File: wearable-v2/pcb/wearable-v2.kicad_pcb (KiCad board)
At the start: 2 copper layers, 112.1 x 40.2 mm, 90 parts, among them IC1 TESEO-LIV3F, J1 HERALD_V2_CONN_RECEPTACLE, J2 HERALD_V2_CONN_RECEPTACLE, J3 HERALD_V2_CONN_RECEPTACLE, J4 HERALD_V2_CONN_RECEPTACLE, J5 HERALD_V2_CONN_PORT, J6 HERALD_V2_CONN_PORT, J7 USB_C_Receptacle_USB2.0, J8 HERALD_V2_CONN_PORT, J9 HERALD_V2_CONN_PORT, SW1 SW_Push, U1 DT1446-04V, U10 ATmega328PB-M, U11 TMP1075, U12 MAX30102, U14 LIS2DE12, U15 TLV751, U2 MCP73831/2-2MC, U3 TCA6408A, U4 FT201XQ, U6 BC833, U7 MX25R8035FZxxx0, U8 PCF85063ATL, U9 APDS-9250, Y1 32.768kHz

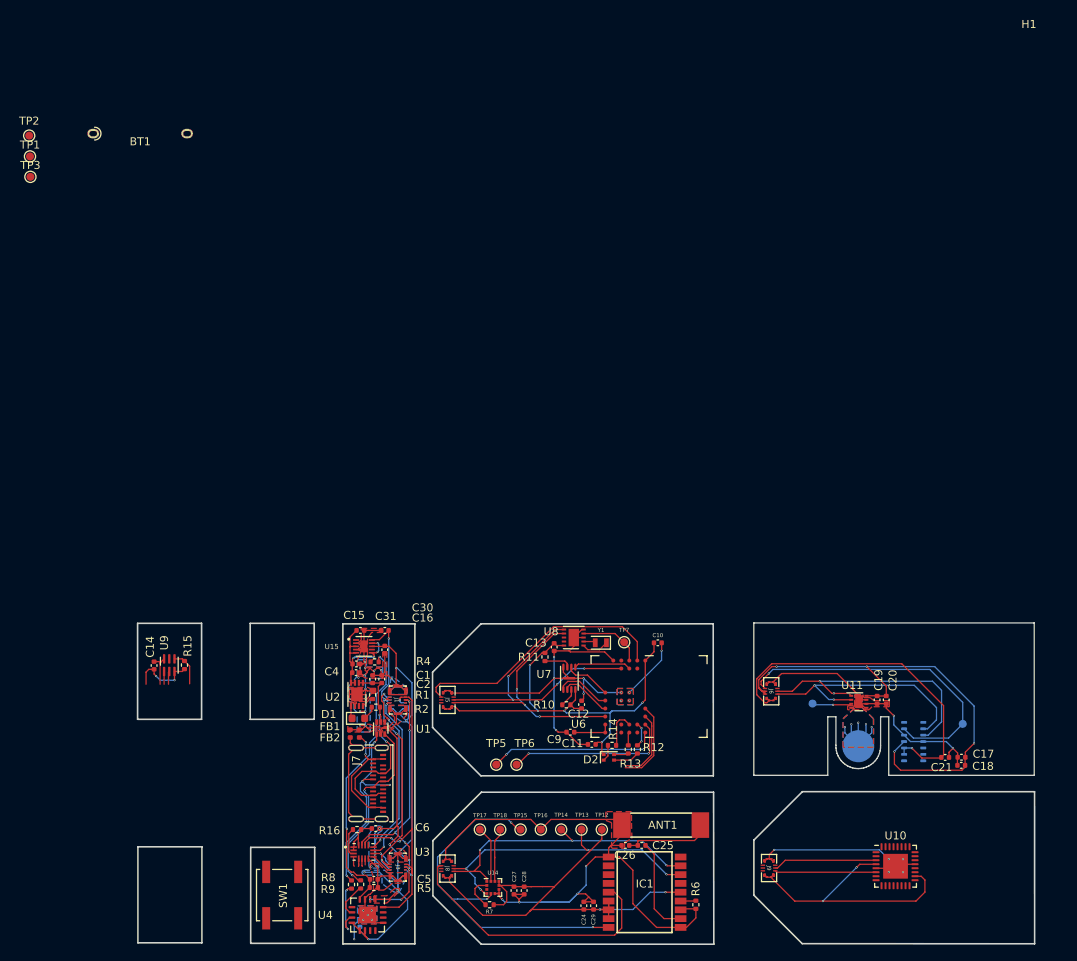
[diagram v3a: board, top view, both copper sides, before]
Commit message: Set wider PCB GND tracks and vias
Signed-off-by: Adam Fowler <adam@adamfowler.org>
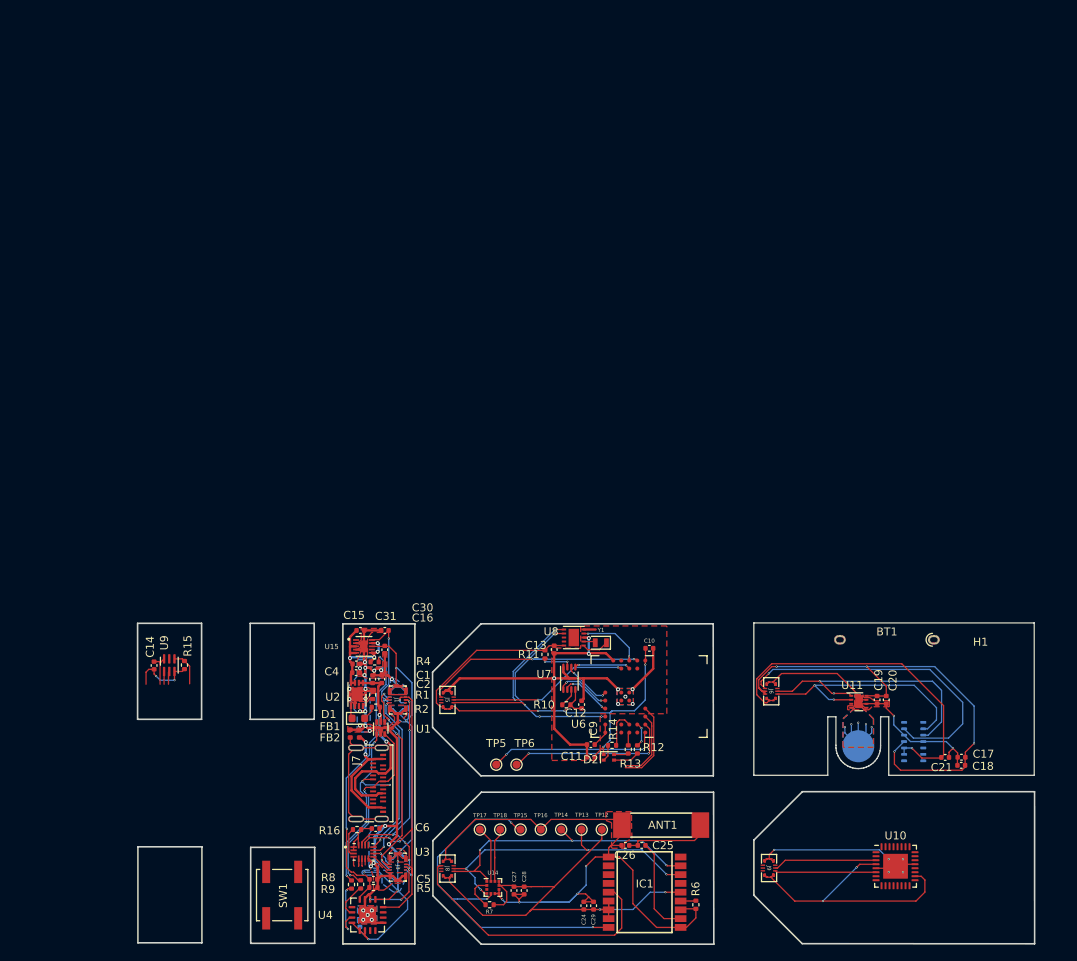
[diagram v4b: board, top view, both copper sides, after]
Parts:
- removed TP1: VBUS, TestPoint:TestPoint_Pad_D1.0mm
- removed TP11: BIOINT, TestPoint:TestPoint_Pad_D1.0mm
- removed TP2: GND, TestPoint:TestPoint_Pad_D1.0mm
- removed TP3: BTSTAT, TestPoint:TestPoint_Pad_D1.0mm
- removed TP7: RTCINT, TestPoint:TestPoint_Pad_D1.0mm
- removed TP8: TMPINT, TestPoint:TestPoint_Pad_D1.0mm
- moved BT1 112.8 mm to (159.3, 101.2), turned to 180 degrees
- moved H1 77.5 mm to (171.0, 103.1)
- moved C9 3.00 mm to (122.3, 114.4)
- moved C11 1.60 mm to (122.3, 115.9)
- moved C10 1.26 mm to (129.6, 102.3)
- moved R11 0.32 mm to (116.5, 103.1)
- moved C13 0.30 mm to (117.7, 102.5)
- moved C5 0.05 mm to (95.1, 131.2)
- moved R5 0.05 mm to (95.1, 132.2)
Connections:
- U8 pad EP: GND -> (no net)
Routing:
- net VDD: track 288.7 -> 297.4 mm, vias 19 -> 18
- net /Bio Board V1/TMP_INT: track 4.95 -> 0.00 mm, vias 1 -> 0
- net GND: track 333.8 -> 329.6 mm, vias 53 -> 49
- net /Compute - Fanstel BC833M - Nordic Semi nRF52833 based/EXT_INT1: track 54.4 -> 50.3 mm, vias 2 -> 4
- net VBUS: track 30.7 -> 28.8 mm
- net /Compute - Fanstel BC833M - Nordic Semi nRF52833 based/FLASH_WP: track 3.38 -> 3.89 mm, vias 0 -> 2
- net /Compute - Fanstel BC833M - Nordic Semi nRF52833 based/MISO: track 5.83 -> 6.21 mm, vias 0 -> 2
- net /Bio Board V1/SCL: track 155.1 -> 155.3 mm, vias 12 -> 13
- net /Compute - Fanstel BC833M - Nordic Semi nRF52833 based/SCLK: track 6.50 -> 6.60 mm, vias 0 -> 2
- net /Compute - Fanstel BC833M - Nordic Semi nRF52833 based/FLASH_CS: track 7.13 -> 7.05 mm, vias 0 -> 2
- net /Compute - Fanstel BC833M - Nordic Semi nRF52833 based/RTC_INT: track 8.04 -> 8.08 mm, vias 0 -> 2
- net /Compute - Fanstel BC833M - Nordic Semi nRF52833 based/MOSI: track 6.93 -> 6.95 mm, vias 0 -> 2

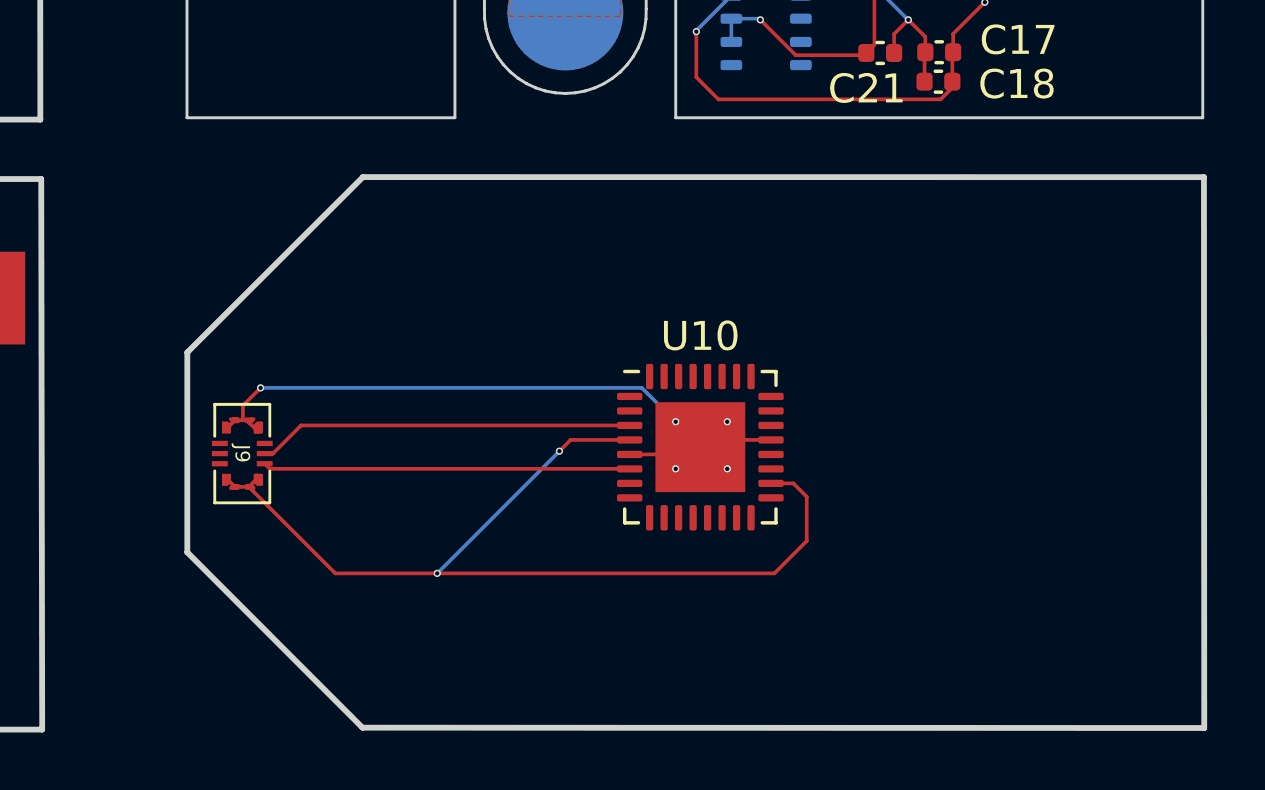
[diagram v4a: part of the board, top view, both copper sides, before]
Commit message: Display board physical layout improvements
Signed-off-by: Adam Fowler <adam@adamfowler.org>
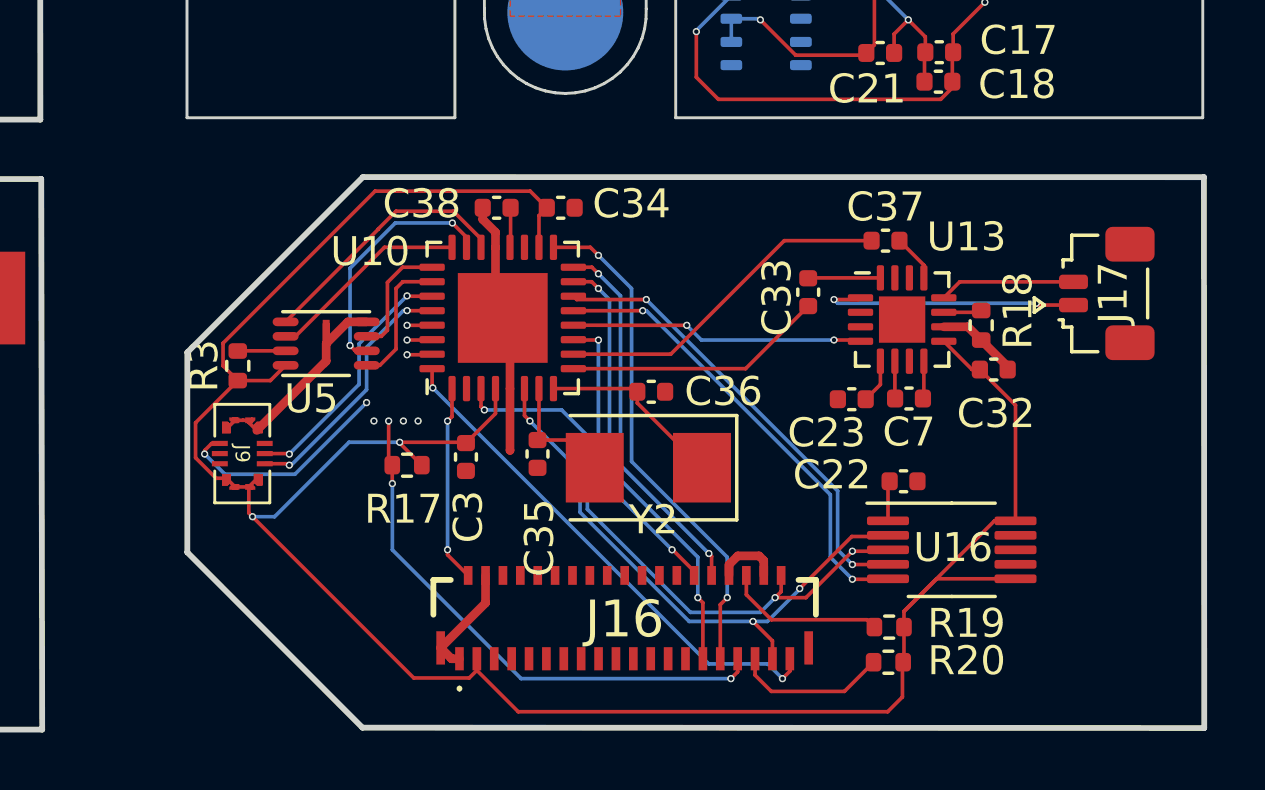
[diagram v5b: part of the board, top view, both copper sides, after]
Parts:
- added C22: 1uF 0402, Capacitor_SMD:C_0402_1005Metric, F.Cu at (167.4, 130.7)
- added C23: 1uF 0402, Capacitor_SMD:C_0402_1005Metric, F.Cu at (165.6, 127.9)
- added C3: 100nF 0402, Capacitor_SMD:C_0402_1005Metric, F.Cu at (152.3, 129.9)
- added C32: 1uF 0402, Capacitor_SMD:C_0402_1005Metric, F.Cu at (170.5, 126.9)
- added C33: 2.2uF 0402, Capacitor_SMD:C_0402_1005Metric, F.Cu at (164.1, 124.2)
- added C34: 10uF 0402, Capacitor_SMD:C_0402_1005Metric, F.Cu at (155.5, 121.3)
- added C35: 22pF 0402, Capacitor_SMD:C_0402_1005Metric, F.Cu at (154.7, 129.8)
- added C36: 22pF 0402, Capacitor_SMD:C_0402_1005Metric, F.Cu at (158.7, 127.6)
- added C37: 2.2uF 0402, Capacitor_SMD:C_0402_1005Metric, F.Cu at (166.8, 122.4)
- added C38: 100nF 0402, Capacitor_SMD:C_0402_1005Metric, F.Cu at (153.3, 121.3)
- added C7: 1uF 0402, Capacitor_SMD:C_0402_1005Metric, F.Cu at (167.6, 127.9)
- added J16: EA_WF030-39S, Herald:EAWF03039S, F.Cu at (157.7, 135.7)
- added J17: Conn_01x02_Pin, Connector_JST:JST_SUR_SM02B-SURS-TF_1x02-1MP_P0.80mm_Horizontal, F.Cu at (174.4, 124.2)
- added R17: 1k 0402, Resistor_SMD:R_0402_1005Metric, F.Cu at (150.2, 130.2)
- added R18: 49.9k 0402, Resistor_SMD:R_0402_1005Metric, F.Cu at (170.1, 125.3)
- added R19: 10k 0402, Resistor_SMD:R_0402_1005Metric, F.Cu at (166.9, 135.8)
- added R20: 10k 0402, Resistor_SMD:R_0402_1005Metric, F.Cu at (166.8, 137.0)
- added R3: 10k, Resistor_SMD:R_0402_1005Metric, F.Cu at (144.4, 126.7)
- added U13: TPA6139A2RGTR, Package_DFN_QFN:TQFN-16-1EP_3x3mm_P0.5mm_EP1.6x1.6mm, F.Cu at (167.3, 125.2)
- added U16: DRV2605LDGS, Package_SO:VSSOP-10_3x3mm_P0.5mm, F.Cu at (169.0, 133.1)
- added U5: MX25R8035FZxxx0, Herald:USON-8-1EP_2x3mm_P0.5mm_EP0.25x1.65mm, F.Cu at (147.4, 126.0)
- added Y2: 8Mhz, Crystal:Crystal_SMD_5032-2Pin_5.0x3.2mm, F.Cu at (158.6, 130.3)
- moved U10 8.15 mm to (153.5, 125.1), turned to 90 degrees
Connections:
- net /Display Board V1/SOUND_PWM renamed /Display Board V1/FB_FTDI_TX
- net /Display Board V1/SS1 renamed /Display Board V1/FB_SS1
- ANT1 pad 2: GND -> (no net)
- J4 pad 6: /Display Board V1/INT_4 -> /Display Board V1/TOUCH_INT
- U10 pad 1: unconnected-(U10-PD3-Pad1) -> /Display Board V1/DISP_LED+
- U10 pad 10: /Display Board V1/VIBRATE_PWM -> /Display Board V1/FB_AUDIO_PWM_RIGHT
- U10 pad 11: unconnected-(U10-PD7-Pad11) -> /Display Board V1/DISP_CSX
- U10 pad 12: unconnected-(U10-PB0-Pad12) -> /Display Board V1/FB_AUDIO_SEL
- U10 pad 13: unconnected-(U10-PB1-Pad13) -> /Display Board V1/FB_VIBRATE_EN
- U10 pad 14: /Display Board V1/CSX -> /Display Board V1/FB_VIBRATE_PWM
- U10 pad 15: /Display Board V1/MOSI0 -> /Display Board V1/DISP_SDA
- U10 pad 16: /Display Board V1/MISO0 -> /Display Board V1/DISP_SDO
- U10 pad 17: /Display Board V1/DCX -> /Display Board V1/DISP_DCX
- U10 pad 20: unconnected-(U10-AREF-Pad20) -> Net-(U10-AREF)
- U10 pad 22: /Display Board V1/MOSI1 -> /Display Board V1/FB_MOSI1
- U10 pad 23: /Display Board V1/MISO1 -> /Display Board V1/FB_MISO1
- U10 pad 24: /Display Board V1/SCK1 -> /Display Board V1/FB_SCK1
- U10 pad 25: /Display Board V1/LED+ -> /Display Board V1/FB_FLASH_WP
- U10 pad 26: unconnected-(U10-PC3-Pad26) -> /Display Board V1/FB_FLASH_SEL
- U10 pad 29: /Display Board V1/AVR_RESET -> /Display Board V1/DISP_RESET
- U10 pad 3: /Bio Board V1/SDA -> /Display Board V1/FB_SDA
- U10 pad 31: unconnected-(U10-PD1-Pad31) -> /Display Board V1/FB_FTDI_RX
- U10 pad 32: /Display Board V1/INT_4 -> /Display Board V1/TOUCH_INT
- U10 pad 6: /Bio Board V1/SCL -> /Display Board V1/FB_SCL
- U10 pad 7: unconnected-(U10-XTAL1/PB6-Pad7) -> Net-(U10-XTAL1/PB6)
- U10 pad 8: unconnected-(U10-XTAL2/PB7-Pad8) -> Net-(U10-XTAL2/PB7)
- U10 pad 9: unconnected-(U10-PD5-Pad9) -> /Display Board V1/FB_AUDIO_PWM_LEFT
- U15 pad 11: GND -> (no net)
- U2 pad 9: GND -> (no net)
- U3 pad 10: /Display Board V1/INT_4 -> /Display Board V1/TOUCH_INT
- U8 pad EP: (no net) -> unconnected-(U8-PadEP)
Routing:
- net VDD: track 297.4 -> 347.3 mm
- net /Display Board V1/FB_SDA: track 0.00 -> 20.9 mm, vias 0 -> 3
- net /Display Board V1/TOUCH_INT: track 0.00 -> 20.5 mm, vias 0 -> 3
- net /Display Board V1/FB_SCL: track 0.00 -> 20.1 mm, vias 0 -> 3
- net /Display Board V1/DISP_RESET: track 0.00 -> 19.7 mm, vias 0 -> 4
- net /Display Board V1/DISP_DCX: track 0.00 -> 17.5 mm, vias 0 -> 2
- net /Display Board V1/FB_VIBRATE_EN: track 0.00 -> 16.0 mm, vias 0 -> 2
- net /Display Board V1/FB_VIBRATE_PWM: track 0.00 -> 15.9 mm, vias 0 -> 2
- net /Display Board V1/DISP_SDA: track 0.00 -> 15.2 mm, vias 0 -> 2
- net /Display Board V1/DISP_SDO: track 0.00 -> 13.0 mm, vias 0 -> 2
- net /Display Board V1/FB_AUDIO_PWM_RIGHT: track 0.00 -> 11.9 mm
- net /Display Board V1/DISP_CSX: track 0.00 -> 10.4 mm, vias 0 -> 2
- net /Display Board V1/FB_AUDIO_SEL: track 0.00 -> 10.1 mm, vias 0 -> 2
- net /Display Board V1/FB_SPEAKER_OUT_LEFT: track 0.00 -> 9.28 mm, vias 0 -> 2
- net /Display Board V1/FB_MOSI1: track 0.00 -> 9.02 mm
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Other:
- board text added: "FTDI Here"

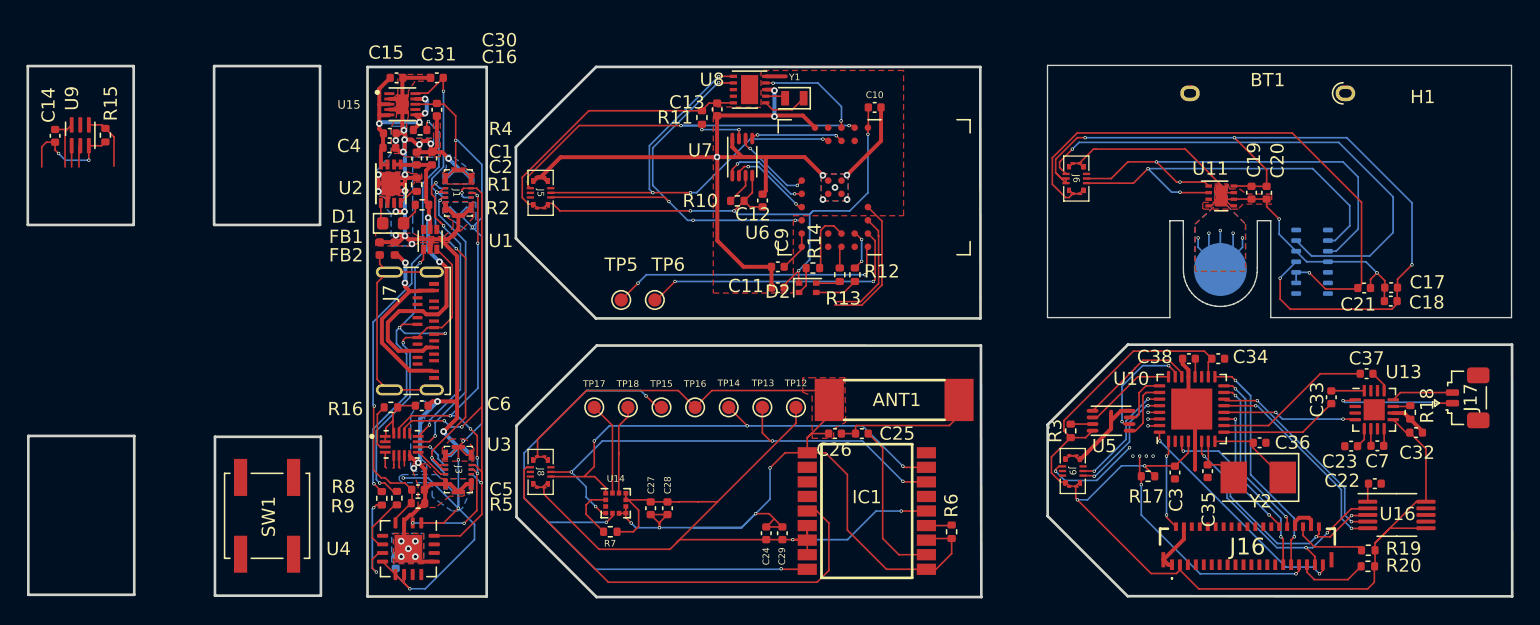
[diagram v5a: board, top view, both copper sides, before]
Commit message: Confirmed display board connectors
Signed-off-by: Adam Fowler <adam@adamfowler.org>
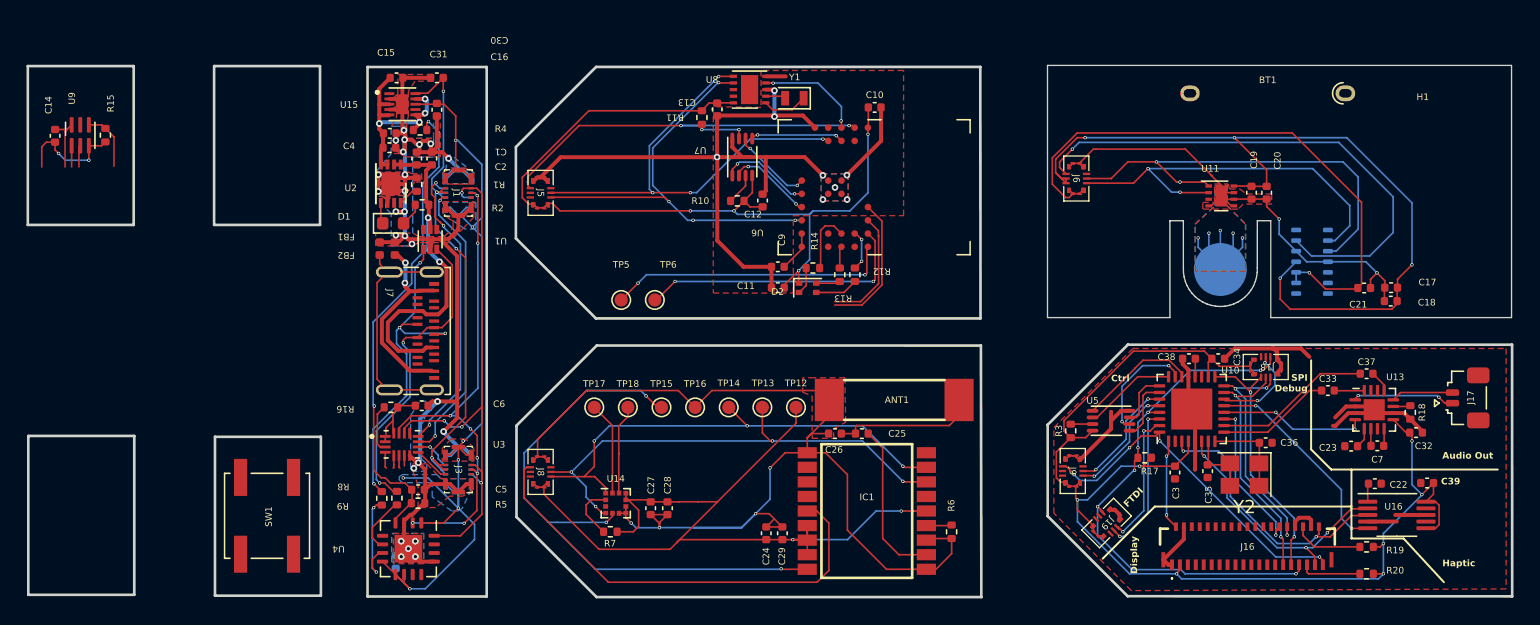
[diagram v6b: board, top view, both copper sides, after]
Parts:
- added C39: 100nF 0402, Capacitor_SMD:C_0402_1005Metric, F.Cu at (171.3, 130.7)
- added J18: DEBUG_HERALD, Herald:HERALD_V2_CONN_PORT, F.Cu at (159.1, 121.9)
- added J19: FTDI_HERALD, Herald:HERALD_V2_CONN_PORT, F.Cu at (147.1, 133.7)
- J17: value Conn_01x02_Pin -> JST_AUDIO_OUT
- U5: value MX25R8035FZxxx0 -> MX25R8035FZUIL0
- Y2: footprint Crystal:Crystal_SMD_5032-2Pin_5.0x3.2mm -> Crystal:Crystal_SMD_3225-4Pin_3.2x2.5mm
- moved R17 1.42 mm to (150.0, 128.8)
- moved Y2 1.07 mm to (157.5, 130.0)
- moved R20 0.57 mm to (166.8, 137.5)
- moved C33 0.57 mm to (163.8, 123.7), turned to 180 degrees
- moved C36 0.46 mm to (159.1, 127.6)
- moved R19 0.28 mm to (166.8, 135.5)
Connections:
- net /Display Board V1/DISP_LED+ renamed /Display Board V1/FB_LED_PWM
- net /Display Board V1/DISP_RESET renamed /Display Board V1/FB_AVR_RESET
- net /Display Board V1/FB_SDA renamed /Display Board V1/FB_SCA
- J16 pad 39: /Display Board V1/TOUCH_INT -> /Display Board V1/FB_INT
- J4 pad 6: /Display Board V1/TOUCH_INT -> /Standard Connector/INT_4
- J9 pad 6: /Display Board V1/INT_4 -> /Display Board V1/FB_INT
- U10 pad 14: /Display Board V1/FB_VIBRATE_PWM -> /Display Board V1/FB_SS0
- U10 pad 30: /Display Board V1/FB_FTDI_TX -> /Display Board V1/FB_TWI_RX
- U10 pad 31: /Display Board V1/FB_FTDI_RX -> /Display Board V1/FB_TWI_TX
- U10 pad 32: /Display Board V1/TOUCH_INT -> /Display Board V1/FB_INT
- U13 pad 17: (no net) -> GND
- U16 pad 4: /Display Board V1/FB_VIBRATE_PWM -> GND
- U3 pad 10: /Display Board V1/TOUCH_INT -> /Standard Connector/INT_4
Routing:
- net /Display Board V1/FB_INT: track 0.00 -> 26.4 mm, vias 0 -> 5
- net GND: track 331.8 -> 355.7 mm
- net /Display Board V1/FB_AVR_RESET: track 19.7 -> 40.6 mm, vias 4 -> 6
- net /Display Board V1/TOUCH_INT: track 20.5 -> 0.00 mm, vias 3 -> 0
- net /Display Board V1/FB_VIBRATE_PWM: track 15.9 -> 0.00 mm, vias 2 -> 0
- net /Display Board V1/FB_TWI_RX: track 0.00 -> 11.4 mm, vias 0 -> 2
- net VDD: track 347.3 -> 358.7 mm, vias 18 -> 23
- net /Display Board V1/FB_TWI_TX: track 0.00 -> 10.2 mm, vias 0 -> 2
- net /Display Board V1/INT_4: track 7.65 -> 0.00 mm, vias 3 -> 0
- net /Display Board V1/FB_SS0: track 0.00 -> 6.88 mm, vias 0 -> 2
- net /Display Board V1/DISP_SDO: track 13.0 -> 17.6 mm, vias 2 -> 3
- net /Display Board V1/DISP_SDA: track 15.2 -> 18.4 mm
- net /Standard Connector/INT_4: track 0.00 -> 2.81 mm
- net /Display Board V1/DISP_DCX: track 17.5 -> 19.1 mm
- net /Display Board V1/FB_SPEAKER_OUT_LEFT: track 9.28 -> 7.77 mm
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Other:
- board text added: "Audio Out"
- board text added: "Ctrl"
- board text added: "Display"
- board text added: "FTDI"
- board text added: "Haptic"
- board text added: "SPI Debug"
- board text removed: "FTDI Here"
